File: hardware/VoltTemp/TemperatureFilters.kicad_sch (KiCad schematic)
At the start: 0 parts

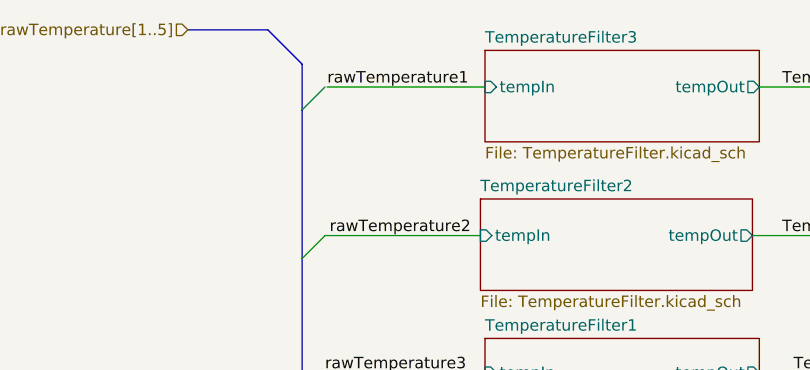
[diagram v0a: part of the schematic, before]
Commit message: changed bild to sharepoint
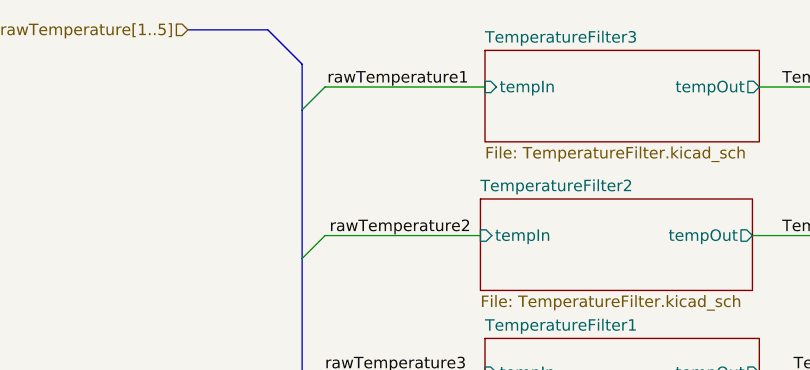
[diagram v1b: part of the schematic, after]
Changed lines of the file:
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@@
+		)
+	)
+	(wire
+		(pts
+			(xy 81.28 66.04) (xy 99.06 66.04)
+		)
+		(stroke
+			(width 0)
+			(type default)
 		)
 	)
@@
 		)
 		(stroke
-			(width 0)
-			(type default)
-		)
-	)
-	(wire
-		(pts
-			(xy 81.534 66.04) (xy 99.06 66.04)
-		)
-		(stroke
